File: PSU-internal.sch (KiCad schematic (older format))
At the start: 56 parts, among them Q3 BD241A

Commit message: Added component numbers.
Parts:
- gave numbers to parts that had none: 48
- renumbered C12 to C1, C8 to C14, C14 to C4, Q3 to Q1, R9 to R1, R12 to R5, R15 to R8

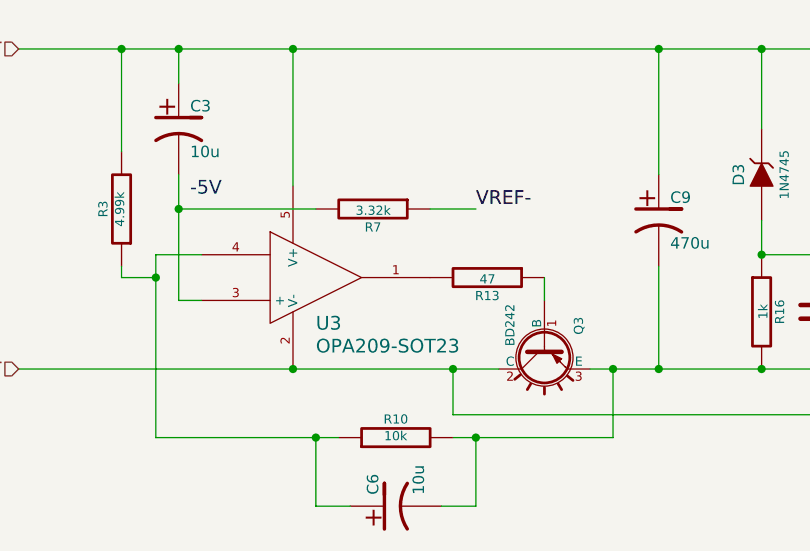
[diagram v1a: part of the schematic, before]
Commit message: Minor schematic mods, started assigning DigiKey part numbers to components.
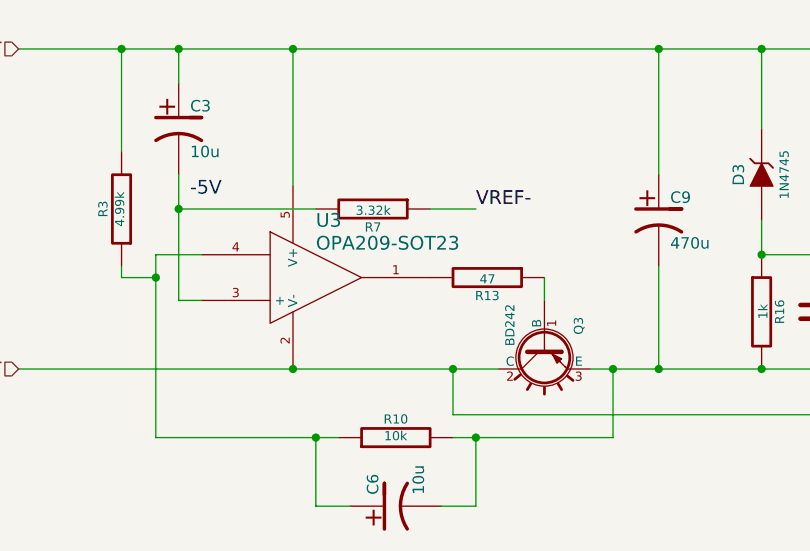
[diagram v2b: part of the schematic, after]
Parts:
- C1, C3: DigiKey (none) -> 493-12772-1-ND
- C10, C11, C12, C18: DigiKey (none) -> 399-4372-ND
- C13, C15, C16, C17, C19, C20: DigiKey (none) -> 445-8425-ND; Note Bypass cap for OpAmp -> (none)
- C2: DigiKey (none) -> 493-12779-1-ND
- C4, C5, C6: DigiKey (none) -> 493-12772-1-ND; Type Tantalum -> (none)
- D1, D3: DigiKey (none) -> 1N4745A-ND
- D2: DigiKey (none) -> 1N4731A-ND
- D4: DigiKey (none) -> 1N4734AFSCT-ND
- Q1, Q2: DigiKey (none) -> BD241CTU-ND
- Q3: DigiKey (none) -> BD242CGOS-ND
- R1, R2, R3: DigiKey (none) -> MFR-25FBF52-4K99
- R10, R8: DigiKey (none) -> MFR-25FBF52-10K
- R11, R12, R13: DigiKey (none) -> S47CACT-ND
- R14, R15, R16, R17: DigiKey (none) -> MFR-25FBF52-1K
- R18, R20, R6: DigiKey (none) -> MFR-25FBF52-1K5
- R19: DigiKey (none) -> MFR-25FBF52-750R
- R4: footprint ~ -> (none); DigiKey (none) -> MFR-25FBF52-1K
- R5, R7: DigiKey (none) -> MFR-25FBF52-3K32
- U1, U2, U3, U9: DigiKey (none) -> 296-28152-1-ND
- U7: DigiKey (none) -> REF02CPZ-ND

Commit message: More components specified
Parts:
- C14, C7, C8, C9: DigiKey (none) -> 493-1084-ND
- R1, R2, R3: DigiKey MFR-25FBF52-4K99 -> 4.99KXBK-ND
- R10, R8: DigiKey MFR-25FBF52-10K -> 10.0KXBK-ND
- R14, R15, R16, R17, R4: DigiKey MFR-25FBF52-1K -> 1.00KXBK-ND
- R18, R20, R6: DigiKey MFR-25FBF52-1K5 -> 1.50KXBK-ND
- R19: DigiKey MFR-25FBF52-750R -> 750XBK-ND
- R5, R7: DigiKey MFR-25FBF52-3K32 -> 3.32KXBK-ND
- R9: DigiKey (none) -> 4.99KXBK-ND
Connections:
- net +5V: now also D4.2 (K)
- net DGND: now also R17.2
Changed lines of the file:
@@
 Sheet 2 6
 Title ""
-Date "23 may 2014"
+Date "25 may 2014"
 Rev ""
 Comp ""
@@
 F 2 "" H 7700 1800 60  0000 C CNN
 F 3 "" H 7700 1800 60  0000 C CNN
+F 4 "493-1084-ND" H 7700 1800 60  0001 C CNN "DigiKey"
 	1    7700 1800
 	1    0    0    -1
@@
 F 2 "~" V 2930 1000 30  0000 C CNN
 F 3 "~" H 3000 1000 30  0000 C CNN
-F 4 "MFR-25FBF52-10K" V 3000 1000 60  0001 C CNN "DigiKey"
+F 4 "10.0KXBK-ND" V 3000 1000 60  0001 C CNN "DigiKey"
 	1    3000 1000
 	0    -1   -1   0
@@
 F 2 "~" V 2830 2000 30  0000 C CNN
 F 3 "~" H 2900 2000 30  0000 C CNN
-F 4 "MFR-25FBF52-3K32" V 2900 2000 60  0001 C CNN "DigiKey"
+F 4 "3.32KXBK-ND" V 2900 2000 60  0001 C CNN "DigiKey"
 	1    2900 2000
 	0    1    1    0
@@
 F 2 "" V 4530 2300 30  0000 C CNN
 F 3 "" H 4600 2300 30  0000 C CNN
-F 4 "MFR-25FBF52-1K" V 4600 2300 60  0001 C CNN "DigiKey"
+F 4 "1.00KXBK-ND" V 4600 2300 60  0001 C CNN "DigiKey"
 	1    4600 2300
 	1    0    0    -1
@@
 F 2 "~" V 2830 6250 30  0000 C CNN
 F 3 "~" H 2900 6250 30  0000 C CNN
-F 4 "MFR-25FBF52-3K32" V 2900 6250 60  0001 C CNN "DigiKey"
+F 4 "3.32KXBK-ND" V 2900 6250 60  0001 C CNN "DigiKey"
 	1    2900 6250
 	0    1    1    0
@@
 $EndComp
 $Comp
-L R R2
-U 1 1 536ECFB3
-P 1800 4350
-F 0 "R2" V 1880 4350 40  0000 C CNN
-F 1 "4.99k" V 1807 4351 40  0000 C CNN
-F 2 "~" V 1730 4350 30  0000 C CNN
-F 3 "~" H 1800 4350 30  0000 C CNN
-F 4 "MFR-25FBF52-4K99" V 1800 4350 60  0001 C CNN "DigiKey"
-	1    1800 4350
-	-1   0    0    1
-$EndComp
-$Comp
 L R R9
 U 1 1 536ECFB9
@@
 F 2 "~" V 2930 3350 30  0000 C CNN
 F 3 "~" H 3000 3350 30  0000 C CNN
+F 4 "4.99KXBK-ND" V 3000 3350 60  0001 C CNN "DigiKey"
 	1    3000 3350
 	0    -1   -1   0
@@
 F 2 "~" V 2830 4350 30  0000 C CNN
 F 3 "~" H 2900 4350 30  0000 C CNN
-F 4 "MFR-25FBF52-1K5" V 2900 4350 60  0001 C CNN "DigiKey"
+F 4 "1.50KXBK-ND" V 2900 4350 60  0001 C CNN "DigiKey"
 	1    2900 4350
 	0    1    1    0
@@
 F 2 "~" V 8730 4100 30  0000 C CNN
 F 3 "~" H 8800 4100 30  0000 C CNN
-F 4 "MFR-25FBF52-750R" V 8800 4100 60  0001 C CNN "DigiKey"
+F 4 "750XBK-ND" V 8800 4100 60  0001 C CNN "DigiKey"
 	1    8800 4100
 	0    1    1    0
@@
 F 2 "" H 4150 1950 60  0000 C CNN
 F 3 "" H 4150 1950 60  0000 C CNN
+F 4 "493-1084-ND" H 4150 1950 60  0001 C CNN "DigiKey"
 	1    4150 1950
 	1    0    0    -1
@@
 F 2 "" H 4150 4300 60  0000 C CNN
 F 3 "" H 4150 4300 60  0000 C CNN
+F 4 "493-1084-ND" H 4150 4300 60  0001 C CNN "DigiKey"
 	1    4150 4300
 	1    0    0    -1
@@
 F 2 "" H 4150 6300 60  0000 C CNN
 F 3 "" H 4150 6300 60  0000 C CNN
+F 4 "493-1084-ND" H 4150 6300 60  0001 C CNN "DigiKey"
 	1    4150 6300
 	1    0    0    -1
@@
 F 2 "~" V 2930 7250 30  0000 C CNN
 F 3 "~" H 3000 7250 30  0000 C CNN
-F 4 "MFR-25FBF52-10K" V 3000 7250 60  0001 C CNN "DigiKey"
+F 4 "10.0KXBK-ND" V 3000 7250 60  0001 C CNN "DigiKey"
 	1    3000 7250
 	0    -1   -1   0
-$EndComp
-$Comp
-L R R17
-U 1 1 537DB15C
-P 8650 2050
-F 0 "R17" V 8730 2050 40  0000 C CNN
-F 1 "1k" V 8657 2051 40  0000 C CNN
-F 2 "" V 8580 2050 30  0000 C CNN
-F 3 "" H 8650 2050 30  0000 C CNN
-F 4 "MFR-25FBF52-1K" V 8650 2050 60  0001 C CNN "DigiKey"
-	1    8650 2050
-	1    0    0    -1
-$EndComp
-$Comp
-L R R15
-U 1 1 537DB169
-P 4600 4650
-F 0 "R15" V 4680 4650 40  0000 C CNN
-F 1 "1k" V 4607 4651 40  0000 C CNN
-F 2 "" V 4530 4650 30  0000 C CNN
-F 3 "" H 4600 4650 30  0000 C CNN
-F 4 "MFR-25FBF52-1K" V 4600 4650 60  0001 C CNN "DigiKey"
-	1    4600 4650
-	1    0    0    -1
-$EndComp
-$Comp
-L R R4
-U 1 1 537DB176
-P 2300 4700
-F 0 "R4" V 2380 4700 40  0000 C CNN
-F 1 "1k" V 2307 4701 40  0000 C CNN
-F 2 "" V 2230 4700 30  0000 C CNN
-F 3 "" H 2300 4700 30  0000 C CNN
-F 4 "MFR-25FBF52-1K" V 2300 4700 60  0001 C CNN "DigiKey"
-	1    2300 4700
-	1    0    0    -1
-$EndComp
-$Comp
-L R R16
-U 1 1 537DB183
-P 4600 6700
-F 0 "R16" V 4680 6700 40  0000 C CNN
-F 1 "1k" V 4607 6701 40  0000 C CNN
-F 2 "" V 4530 6700 30  0000 C CNN
-F 3 "" H 4600 6700 30  0000 C CNN
-F 4 "MFR-25FBF52-1K" V 4600 6700 60  0001 C CNN "DigiKey"
-	1    4600 6700
-	1    0    0    -1
-$EndComp
-$Comp
-L R R3
-U 1 1 537DB1A6
-P 1800 6250
-F 0 "R3" V 1880 6250 40  0000 C CNN
-F 1 "4.99k" V 1807 6251 40  0000 C CNN
-F 2 "~" V 1730 6250 30  0000 C CNN
-F 3 "~" H 1800 6250 30  0000 C CNN
-F 4 "MFR-25FBF52-4K99" V 1800 6250 60  0001 C CNN "DigiKey"
-	1    1800 6250
-	-1   0    0    1
-$EndComp
-$Comp
-L R R1
-U 1 1 537DB1BF
-P 1800 2000
-F 0 "R1" V 1880 2000 40  0000 C CNN
-F 1 "4.99k" V 1807 2001 40  0000 C CNN
-F 2 "~" V 1730 2000 30  0000 C CNN
-F 3 "~" H 1800 2000 30  0000 C CNN
-F 4 "MFR-25FBF52-4K99" V 1800 2000 60  0001 C CNN "DigiKey"
-	1    1800 2000
-	-1   0    0    1
-$EndComp
-$Comp
-L R R20
-U 1 1 537DB201
-P 9700 3300
-F 0 "R20" V 9780 3300 40  0000 C CNN
-F 1 "1.5k" V 9707 3301 40  0000 C CNN
-F 2 "~" V 9630 3300 30  0000 C CNN
-F 3 "~" H 9700 3300 30  0000 C CNN
-F 4 "MFR-25FBF52-1K5" V 9700 3300 60  0001 C CNN "DigiKey"
-	1    9700 3300
-	0    1    1    0
-$EndComp
-$Comp
-L R R18
-U 1 1 537DB21A
-P 8800 3900
-F 0 "R18" V 8880 3900 40  0000 C CNN
-F 1 "1.5k" V 8807 3901 40  0000 C CNN
-F 2 "~" V 8730 3900 30  0000 C CNN
-F 3 "~" H 8800 3900 30  0000 C CNN
-F 4 "MFR-25FBF52-1K5" V 8800 3900 60  0001 C CNN "DigiKey"
-	1    8800 3900
-	0    1    1    0
 $EndComp
 $Comp
@@
 	0    1    1    0
 $EndComp
+Connection ~ 8650 2300
+Connection ~ 8650 1300
+$Comp
+L R R2
+U 1 1 53803BF3
+P 1800 4350
+F 0 "R2" V 1880 4350 40  0000 C CNN
+F 1 "4.99k" V 1807 4351 40  0000 C CNN
+F 2 "~" V 1730 4350 30  0000 C CNN
+F 3 "~" H 1800 4350 30  0000 C CNN
+F 4 "4.99KXBK-ND" V 1800 4350 60  0001 C CNN "DigiKey"
+	1    1800 4350
+	-1   0    0    1
+$EndComp
+$Comp
+L R R1
+U 1 1 53803C06
+P 1800 2000
+F 0 "R1" V 1880 2000 40  0000 C CNN
+F 1 "4.99k" V 1807 2001 40  0000 C CNN
+F 2 "~" V 1730 2000 30  0000 C CNN
+F 3 "~" H 1800 2000 30  0000 C CNN
+F 4 "4.99KXBK-ND" V 1800 2000 60  0001 C CNN "DigiKey"
+	1    1800 2000
+	-1   0    0    1
+$EndComp
+$Comp
+L R R3
+U 1 1 53803C19
+P 1800 6250
+F 0 "R3" V 1880 6250 40  0000 C CNN
+F 1 "4.99k" V 1807 6251 40  0000 C CNN
+F 2 "~" V 1730 6250 30  0000 C CNN
+F 3 "~" H 1800 6250 30  0000 C CNN
+F 4 "4.99KXBK-ND" V 1800 6250 60  0001 C CNN "DigiKey"
+	1    1800 6250
+	-1   0    0    1
+$EndComp
+$Comp
+L R R15
+U 1 1 53803C3E
+P 4600 4650
+F 0 "R15" V 4680 4650 40  0000 C CNN
+F 1 "1k" V 4607 4651 40  0000 C CNN
+F 2 "" V 4530 4650 30  0000 C CNN
+F 3 "" H 4600 4650 30  0000 C CNN
+F 4 "1.00KXBK-ND" V 4600 4650 60  0001 C CNN "DigiKey"
+	1    4600 4650
+	1    0    0    -1
+$EndComp
+$Comp
+L R R16
+U 1 1 53803C45
+P 4600 6700
+F 0 "R16" V 4680 6700 40  0000 C CNN
+F 1 "1k" V 4607 6701 40  0000 C CNN
+F 2 "" V 4530 6700 30  0000 C CNN
+F 3 "" H 4600 6700 30  0000 C CNN
+F 4 "1.00KXBK-ND" V 4600 6700 60  0001 C CNN "DigiKey"
+	1    4600 6700
+	1    0    0    -1
+$EndComp
+$Comp
+L R R17
+U 1 1 53803C4C
+P 8650 2050
+F 0 "R17" V 8730 2050 40  0000 C CNN
+F 1 "1k" V 8657 2051 40  0000 C CNN
+F 2 "" V 8580 2050 30  0000 C CNN
+F 3 "" H 8650 2050 30  0000 C CNN
+F 4 "1.00KXBK-ND" V 8650 2050 60  0001 C CNN "DigiKey"
+	1    8650 2050
+	1    0    0    -1
+$EndComp
+$Comp
+L R R4
+U 1 1 53803DF2
+P 2300 4700
+F 0 "R4" V 2380 4700 40  0000 C CNN
+F 1 "1k" V 2307 4701 40  0000 C CNN
+F 2 "" V 2230 4700 30  0000 C CNN
+F 3 "" H 2300 4700 30  0000 C CNN
+F 4 "1.00KXBK-ND" V 2300 4700 60  0001 C CNN "DigiKey"
+	1    2300 4700
+	1    0    0    -1
+$EndComp
+$Comp
+L R R18
+U 1 1 53803F9E
+P 8800 3900
+F 0 "R18" V 8880 3900 40  0000 C CNN
+F 1 "1.5k" V 8807 3901 40  0000 C CNN
+F 2 "~" V 8730 3900 30  0000 C CNN
+F 3 "~" H 8800 3900 30  0000 C CNN
+F 4 "1.50KXBK-ND" V 8800 3900 60  0001 C CNN "DigiKey"
+	1    8800 3900
+	0    1    1    0
+$EndComp
+$Comp
+L R R20
+U 1 1 53803FB1
+P 9700 3300
+F 0 "R20" V 9780 3300 40  0000 C CNN
+F 1 "1.5k" V 9707 3301 40  0000 C CNN
+F 2 "~" V 9630 3300 30  0000 C CNN
+F 3 "~" H 9700 3300 30  0000 C CNN
+F 4 "1.50KXBK-ND" V 9700 3300 60  0001 C CNN "DigiKey"
+	1    9700 3300
+	0    1    1    0
+$EndComp

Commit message: More footprint specification and connector additions; almost done.
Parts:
- C1, C2, C3, C4, C5, C6: footprint (none) -> Capacitors_Elko_ThroughHole:Elko_vert_DM5_RM2
- C10, C11, C12, C18: footprint (none) -> Capacitors_ThroughHole:Capacitor7.5MMDiscRM5
- C13, C15, C16, C17, C19, C20: footprint (none) -> Capacitors_ThroughHole:Capacitor3MMDiscRM2.5
- C14, C7, C8, C9: footprint (none) -> Capacitors_ThroughHole:Capacitor10x16RM5
- D1, D2, D3, D4: footprint (none) -> Diodes_ThroughHole:Diode_DO-41_SOD81_Horizontal_RM10
- Q1, Q2: footprint TO-220 -> Transistors_TO-220:TO-220_Neutral123_Vertical_LargePads
- Q3: footprint TO220 -> Transistors_TO-220:TO-220_Neutral123_Vertical_LargePads
- R1, R10, R18, R19, R2, R20, R3, R5, R6, R7, R8, R9: footprint ~ -> Resistors_ThroughHole:Resistor_Horizontal_RM10mm
- R11, R12, R13, R14, R15, R16, R17, R4: footprint (none) -> Resistors_ThroughHole:Resistor_Horizontal_RM10mm
- U1, U2, U3, U9: footprint (none) -> SMD_Packages:SOT23-5
- U4, U5, U6, U8: footprint TO-220AB -> Transistors_TO-220:TO-220_Neutral123_Vertical_LargePads
- U7: footprint (none) -> Sockets_DIP:DIP-8__300_ELL

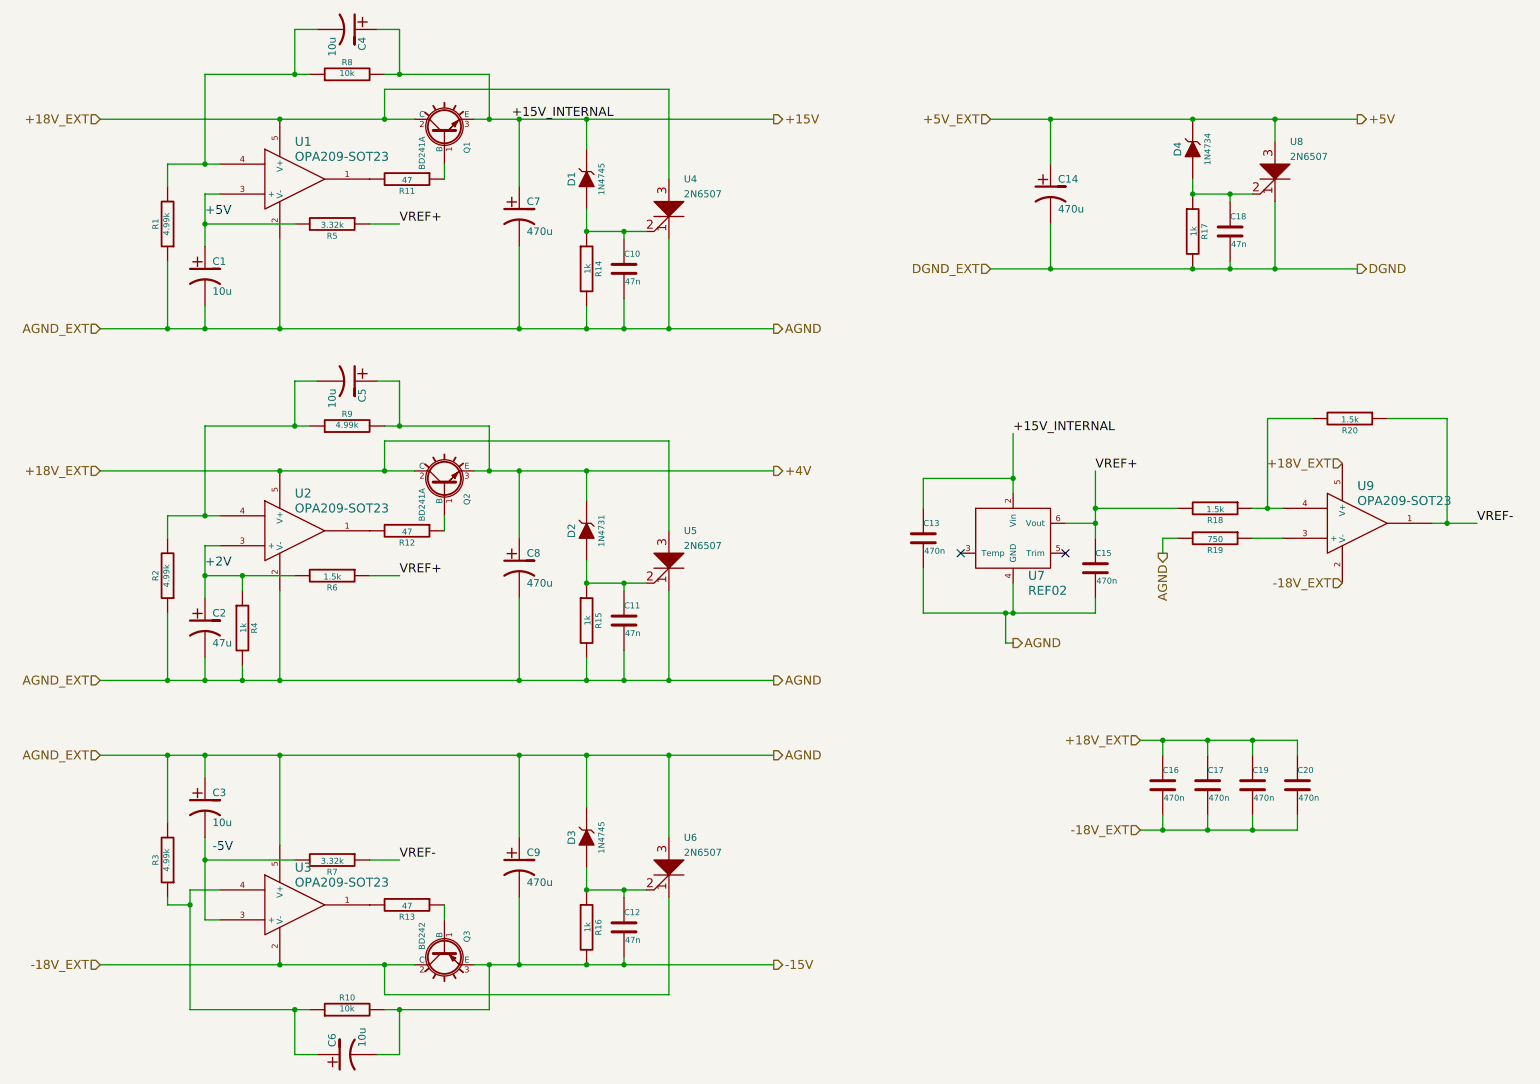
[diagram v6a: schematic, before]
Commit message: A lot of routing, some parts changes:   * Added snubber C/RC snubbers to transformer secondaries.   * Changed PSU OA from OPA209 to OPA27.   * Routed external PSU.   * Mostly done routing internal circuits.  Just need to get everything together.   * Changed digital transformer to a more appropriately-specced one.
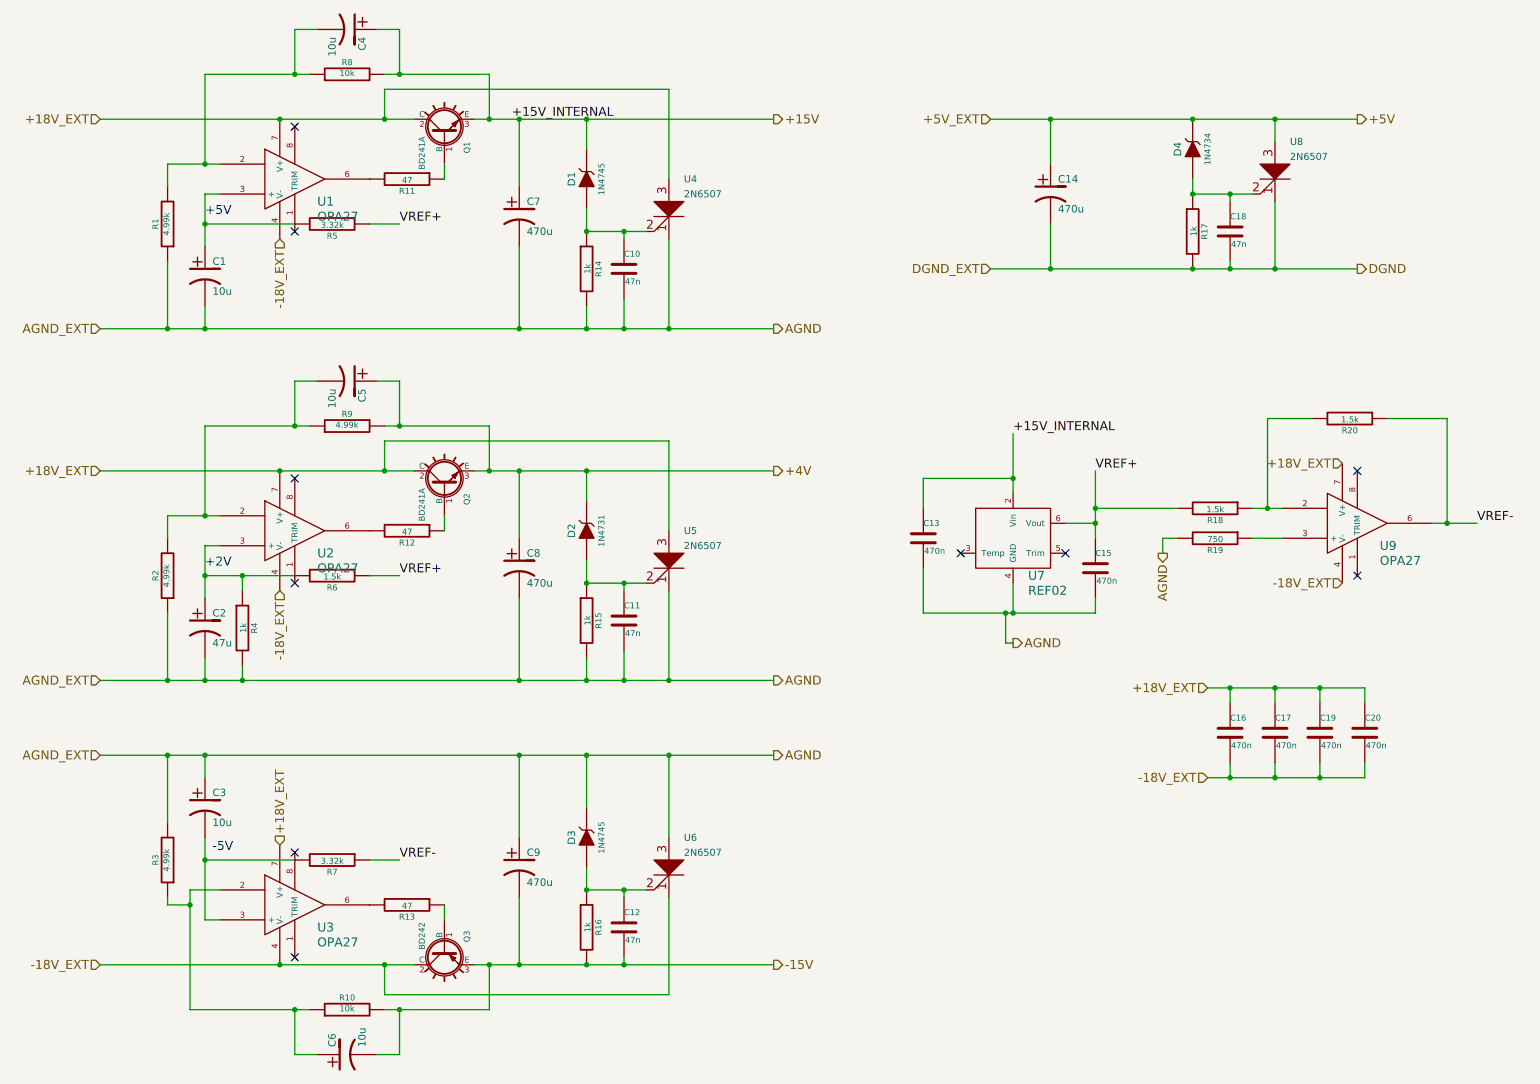
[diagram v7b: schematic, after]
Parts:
- removed U1, U2, U3, U9: OPA209-SOT23, SMD_Packages:SOT23-5, symbol OPA209-SOT23
- added U1, U2, U3, U9: OPA27, Sockets_DIP:DIP-8__300_ELL, symbol OPA27
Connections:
- net +18V_EXT: now also U1.7 (V+), U2.7 (V+), U3.7 (V+), U9.7 (V+)
- net -18V_EXT: now also U1.4 (V-), U2.4 (V-), U3.4 (V-), U9.4 (V-)
- net VREF-: now also U9.6
- net at C4.2, R1.2, R8.1: now also U1.2
- net at C1.1, R5.2: now also U1.3 (+)
- net at R11.2: now also U1.6
- net at C3.2, R7.2: now also U3.3 (+)
- net at R12.2: now also U2.6
- net at C5.2, R2.2, R9.1: now also U2.2
- net at C2.1, R4.1, R6.2: now also U2.3 (+)
- net at R19.1: now also U9.3 (+)
- net at C6.1, R10.1, R3.1: now also U3.2
- net at R13.2: now also U3.6
- net at R18.1, R20.2: now also U9.2
- no-connect marks 2 -> 10
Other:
- moved on the sheet: C16, C17, C19, C20
